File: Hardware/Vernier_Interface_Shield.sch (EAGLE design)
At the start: 36 parts, among them U1 74HC4052SO, U2 LMV358

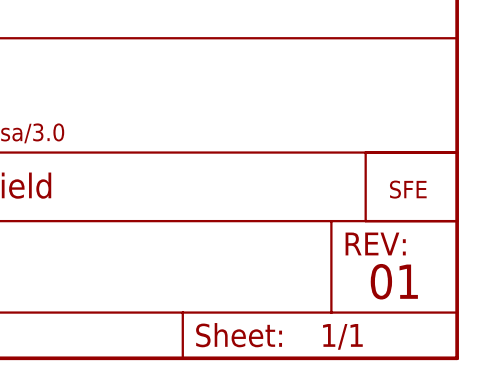
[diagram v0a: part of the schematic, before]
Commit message: Tweaks towards v02
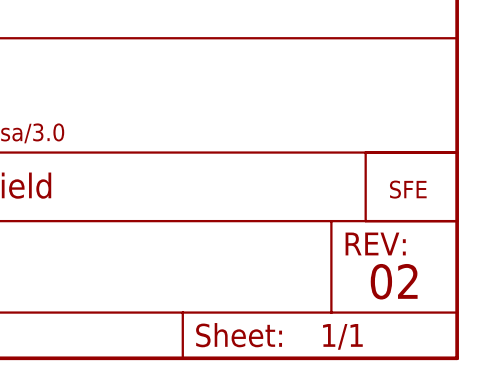
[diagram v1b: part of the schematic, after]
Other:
- note added: "02"
- note removed: "01"
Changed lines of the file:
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@@
 <text x="5.08" y="17.78" size="2.54" layer="91" rot="R90">DIG 2</text>
 <text x="170.942" y="7.62" size="3.81" layer="94">M. Hord</text>
-<text x="239.014" y="6.604" size="3.81" layer="94">01</text>
+<text x="239.014" y="6.604" size="3.81" layer="94">02</text>
 </plain>
 <instances>

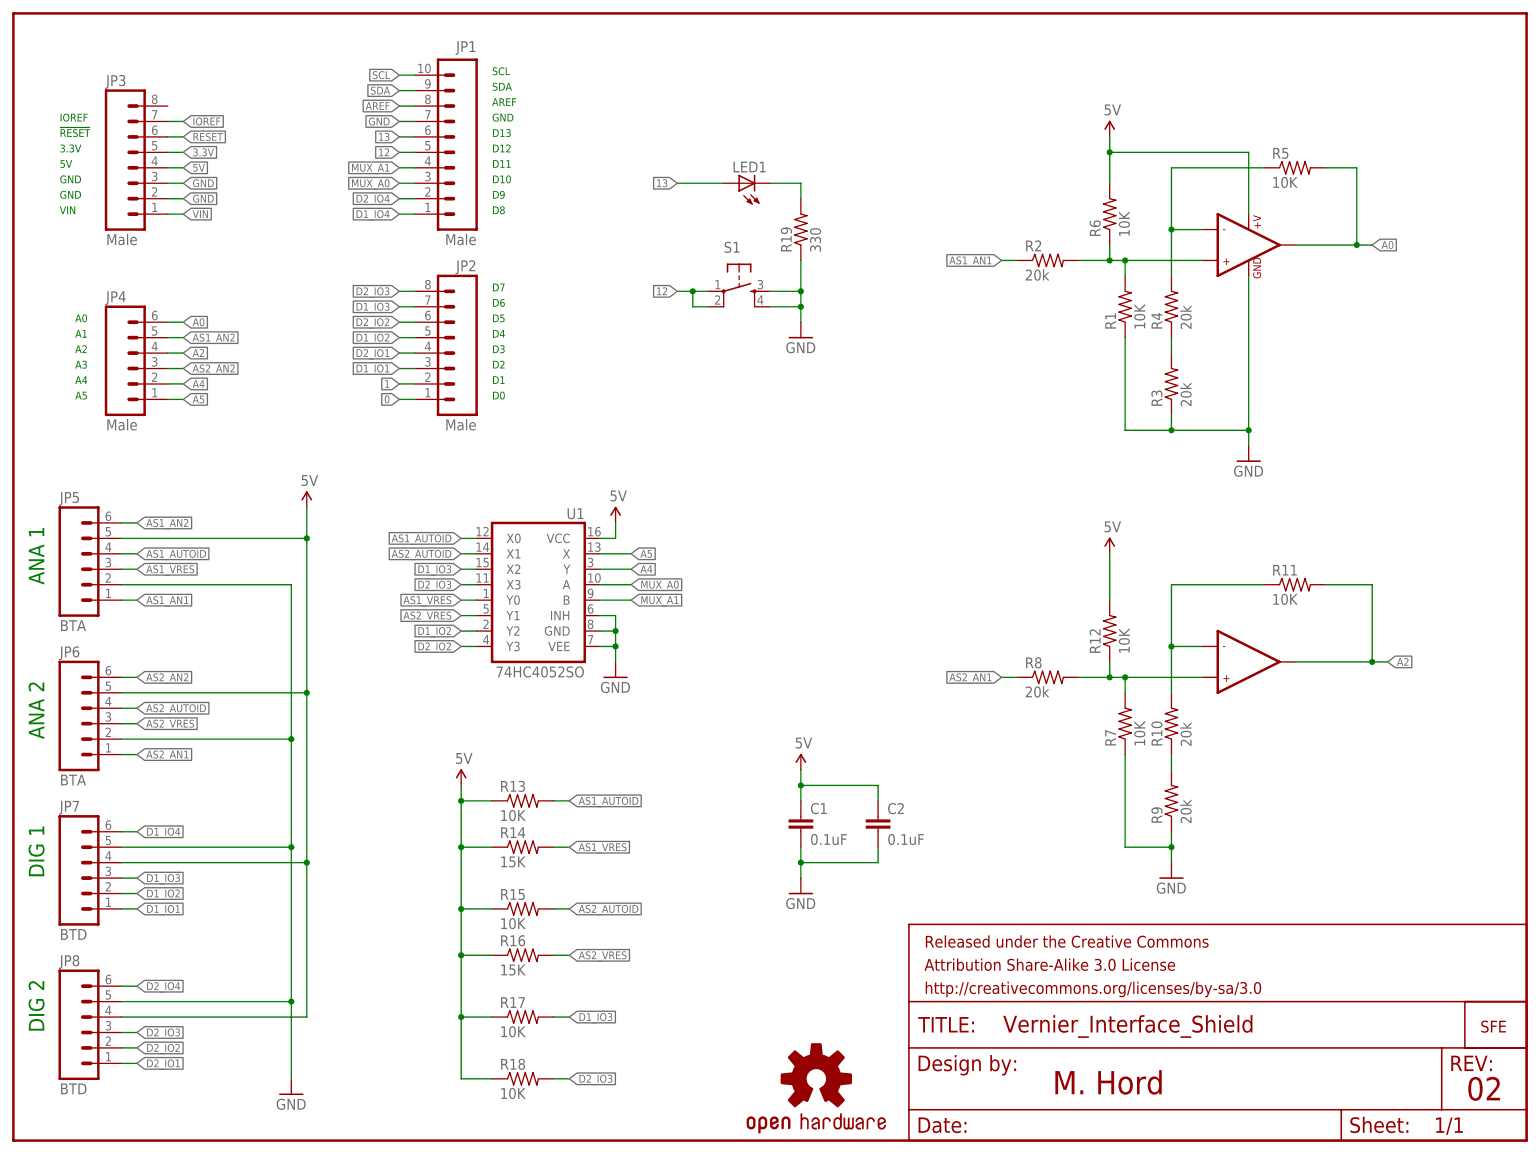
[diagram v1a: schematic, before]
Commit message: Updated footprints of BTA and BTD
Fixed the footprints of BTA and BTD.
Corrected the BTD pin numbering.
Rotated the design so that the connectors don't short out on the USB
cage.
V03
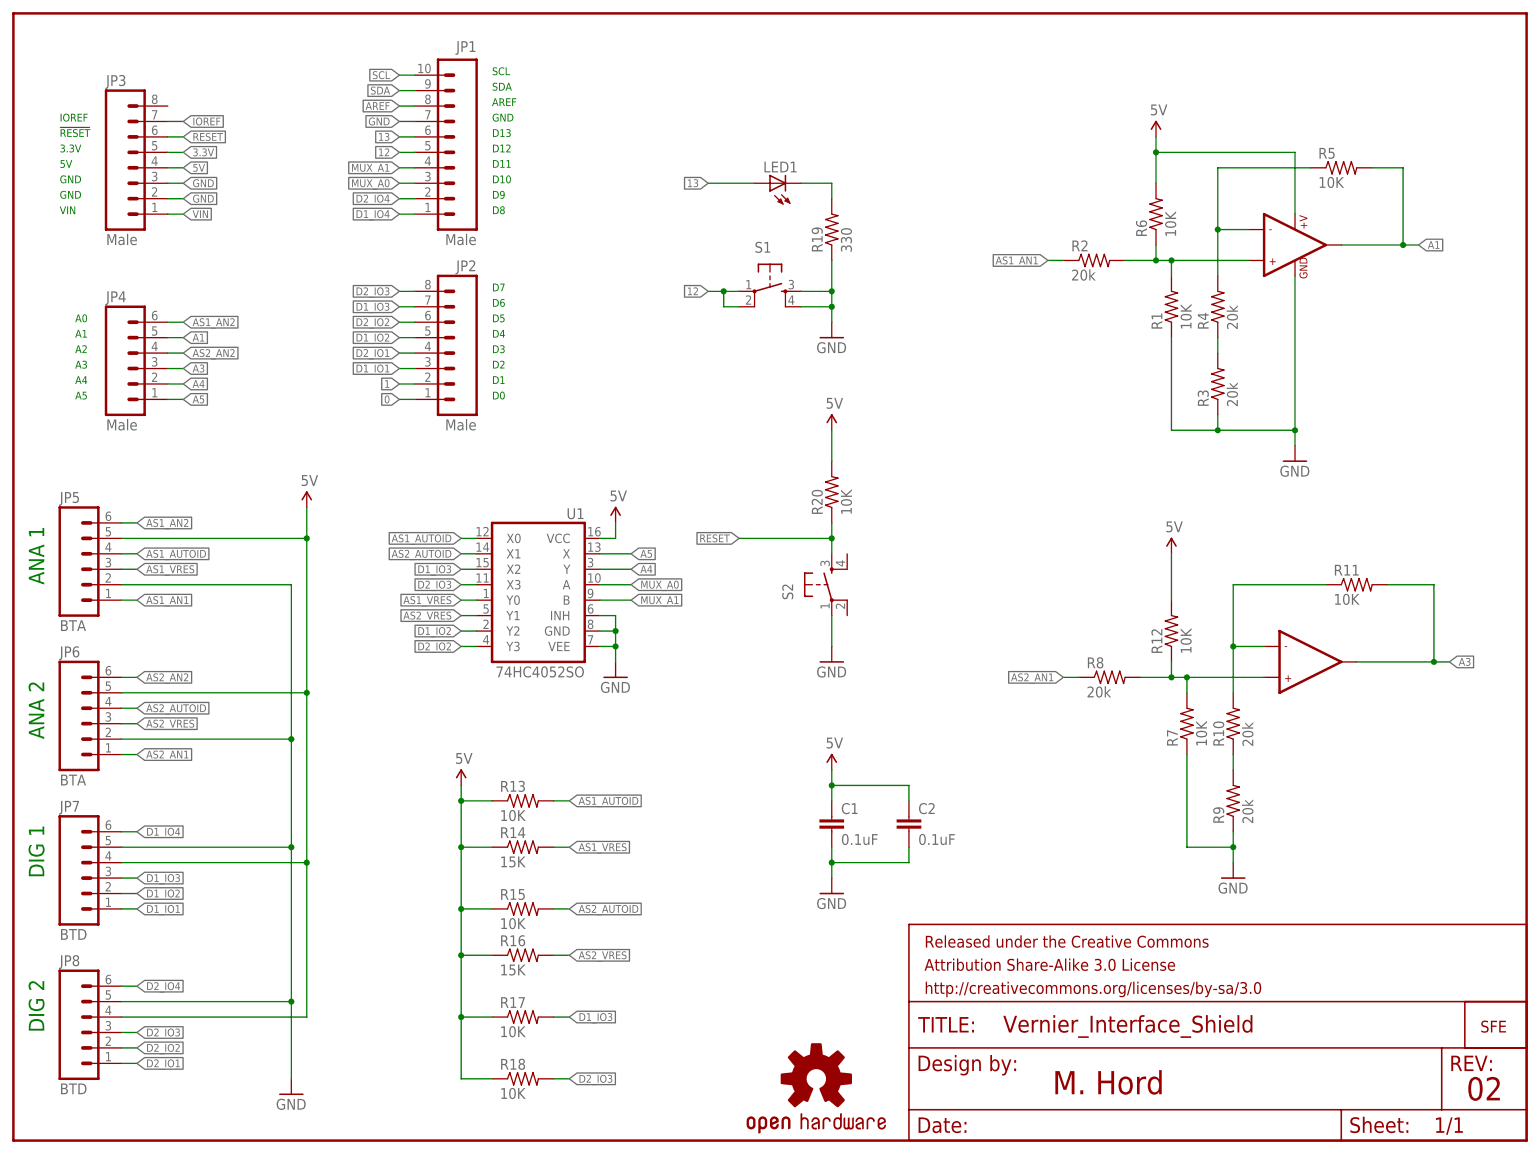
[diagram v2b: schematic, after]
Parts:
- added R20: 10K, SparkFun-Resistors:10KOHM1/10W1%(0603)0603
- added S2: (no value), SparkFun-Electromechanical:TAC_SWITCHPTH
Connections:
- removed net A0: JP4.6, R5.2, U2G$1.OUT1
- removed net A2: JP4.4, R11.2, U2G$2.OUT2
- new net A1: JP4.5, R5.2, U2G$1.OUT1
- new net A3: JP4.3, R11.2, U2G$2.OUT2
- net 5V: now also R20.2
- net AS1_AN2: now also JP4.6; no longer JP4.5
- net AS2_AN2: now also JP4.4; no longer JP4.3
- net GND: now also S2.1
- net RESET: now also R20.1, S2.3
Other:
- moved on the sheet: C1, C2, LED1, R1, R10, R11, R12, R19, R2, R3, R4, R5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

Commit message: Fixed traces, ran DRC, etc...
Updated traces, fixed errors in DRC... more tweaks toward v02
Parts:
- added JP10, JP9: (no value), SparkFun-Connectors:M031X03_NO_SILK
- added JP11: M021X02_NO_SILK, SparkFun-Connectors:M021X02_NO_SILK
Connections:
- net 0: now also JP11.2
- net 1: now also JP11.1
- net 12: now also JP10.1
- net 13: now also JP10.2
- net 5V: now also JP9.1
- net GND: now also JP10.3, JP9.2, JP9.3
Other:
- moved on the sheet: LED1, R1, R10, R11, R12, R13, R14, R15, R16, R17, R18, R19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

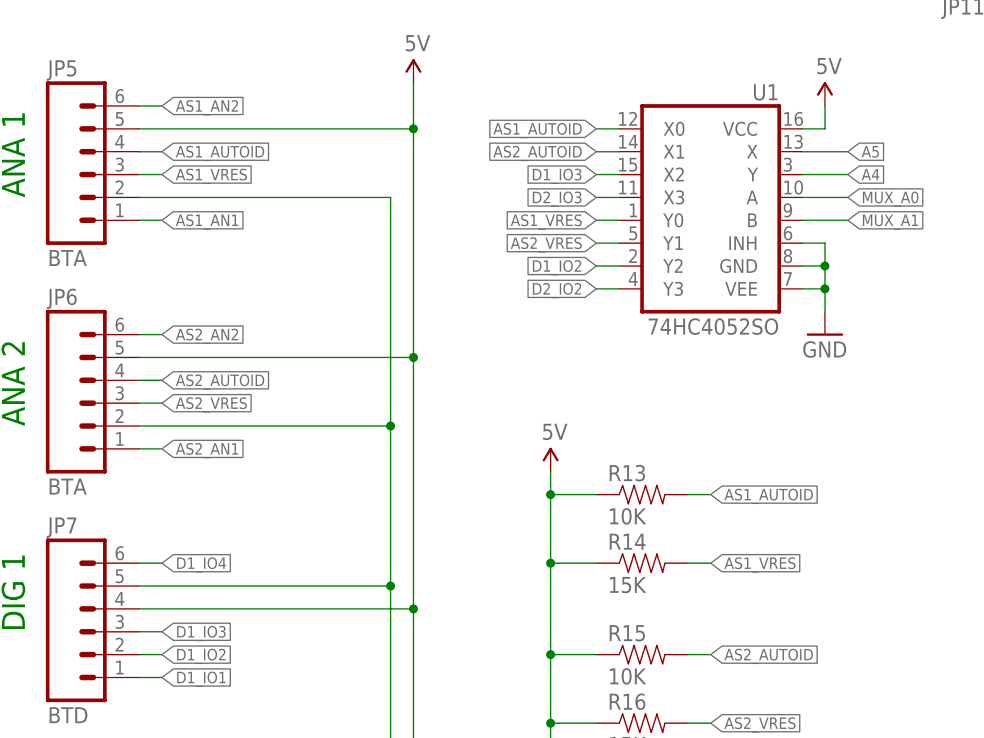
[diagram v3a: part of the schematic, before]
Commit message: addtl clean-up: corrected resistor spacing
Corrected resistor spacing and cleaned-up resulting traces.
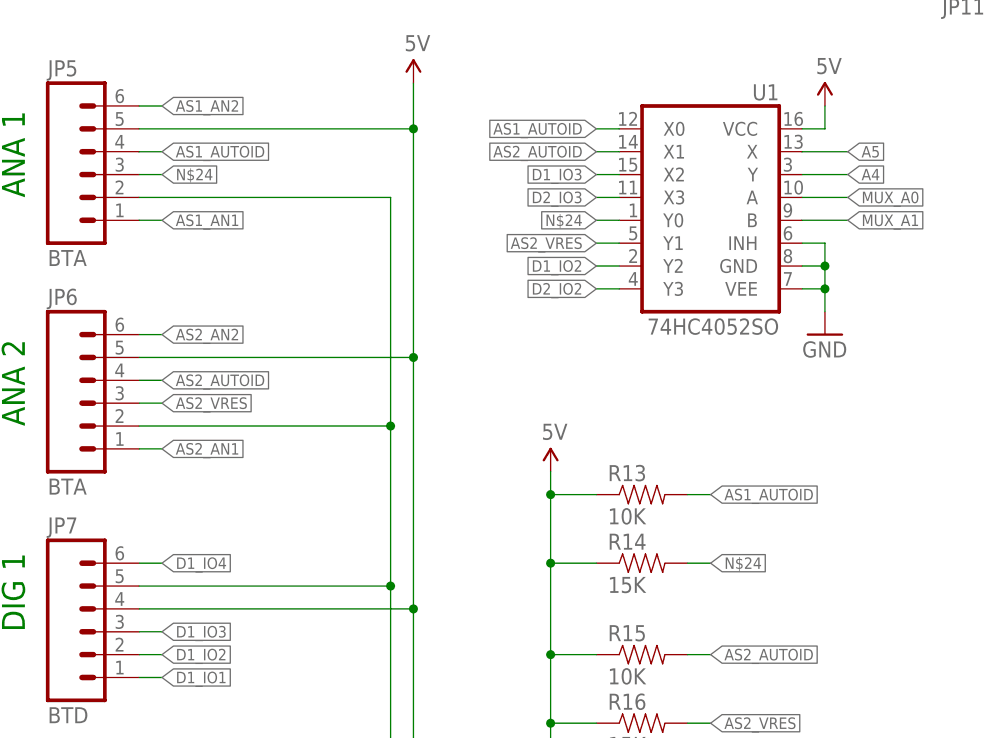
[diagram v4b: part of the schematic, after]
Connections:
- net AS1_VRES renamed N$24
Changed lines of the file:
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@@
 <setting verticaltext="up"/>
 </settings>
-<grid distance="0.05" unitdist="inch" unit="inch" style="lines" multiple="1" display="yes" altdistance="0.005" altunitdist="inch" altunit="inch"/>
+<grid distance="0.1" unitdist="inch" unit="inch" style="lines" multiple="1" display="no" altdistance="0.01" altunitdist="inch" altunit="inch"/>
 <layers>
 <layer number="1" name="Top" color="4" fill="1" visible="no" active="no"/>
@@
 </segment>
 </net>
-<net name="AS1_VRES" class="0">
+<net name="N$24" class="0">
 <segment>
 <wire x1="17.78" y1="93.98" x2="20.32" y2="93.98" width="0.1524" layer="91"/>
